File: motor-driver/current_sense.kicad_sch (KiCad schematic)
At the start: 2 parts, among them U19 INA240A1PWR

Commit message: routing complete
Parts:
- C_bypass2: renamed from C_bypass1; footprint (none) -> Capacitor_SMD:C_0603_1608Metric
- renumbered U19 to U20
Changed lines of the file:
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@@
 		(dnp no)
 		(fields_autoplaced yes)
-		(property "Reference" "C_bypass1"
+		(property "Reference" "C_bypass2"
 			(at 194.31 90.1699 0)
 			(effects
@@
 			)
 		)
-		(property "Footprint" ""
+		(property "Footprint" "Capacitor_SMD:C_0603_1608Metric"
 			(at 191.4652 95.25 0)
 			(effects
@@
 			(project "motor-driver"
 				(path "/2980fc7e-b297-4843-ba9f-cceafa384b2f/d36b7053-ee22-4492-bdec-8a6a56460e2b/66c4064f-6677-423e-92fa-0fdb45cd4b17"
-					(reference "C_bypass1")
+					(reference "C_bypass2")
 					(unit 1)
 				)
 				(path "/2980fc7e-b297-4843-ba9f-cceafa384b2f/d36b7053-ee22-4492-bdec-8a6a56460e2b/7d8ebe4c-0ee3-4602-8190-2918d9e2b81c"
-					(reference "C_bypass2")
+					(reference "C_bypass3")
 					(unit 1)
 				)
@@
 		(dnp no)
 		(fields_autoplaced yes)
-		(property "Reference" "U19"
+		(property "Reference" "U20"
 			(at 153.67 86.6392 0)
 			(effects
@@
 			(project "motor-driver"
 				(path "/2980fc7e-b297-4843-ba9f-cceafa384b2f/d36b7053-ee22-4492-bdec-8a6a56460e2b/66c4064f-6677-423e-92fa-0fdb45cd4b17"
-					(reference "U19")
+					(reference "U20")
 					(unit 1)
 				)
 				(path "/2980fc7e-b297-4843-ba9f-cceafa384b2f/d36b7053-ee22-4492-bdec-8a6a56460e2b/7d8ebe4c-0ee3-4602-8190-2918d9e2b81c"
-					(reference "U20")
-					(unit 1)
-				)
+					(reference "U21")
+					(unit 1)
+				)

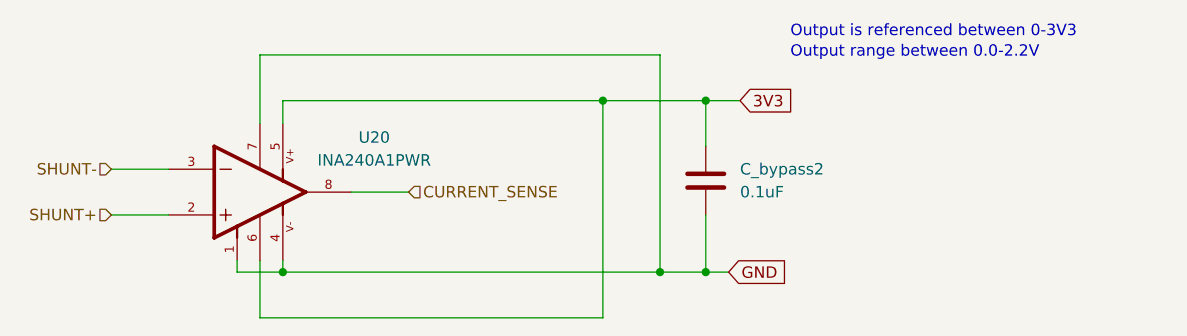
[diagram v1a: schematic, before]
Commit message: added spi connection
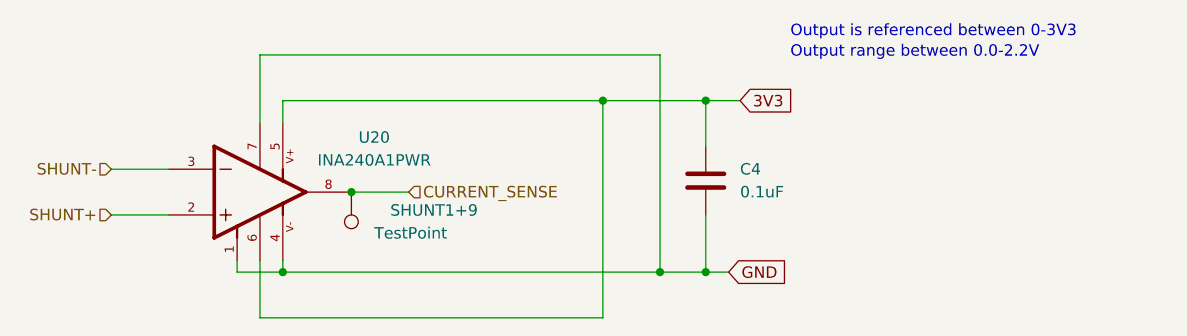
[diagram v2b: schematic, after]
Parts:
- added SHUNT1+9: TestPoint, TestPoint:TestPoint_Loop_D1.80mm_Drill1.0mm_Beaded, symbol Connector:TestPoint
- renumbered C_bypass2 to C4
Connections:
- net CURRENT_SENSE: now also SHUNT1+9.1
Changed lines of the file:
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@@
+	)
+	(junction
+		(at 151.13 92.71)
+		(diameter 0)
+		(color 0 0 0 0)
 	)
 	(junction
@@
 		(dnp no)
 		(fields_autoplaced yes)
-		(property "Reference" "C_bypass2"
+		(property "Reference" "C4"
 			(at 194.31 90.1699 0)
 			(effects
@@
 			(project "motor-driver"
 				(path "/2980fc7e-b297-4843-ba9f-cceafa384b2f/d36b7053-ee22-4492-bdec-8a6a56460e2b/66c4064f-6677-423e-92fa-0fdb45cd4b17"
-					(reference "C_bypass2")
+					(reference "C4")
 					(unit 1)
 				)
 				(path "/2980fc7e-b297-4843-ba9f-cceafa384b2f/d36b7053-ee22-4492-bdec-8a6a56460e2b/7d8ebe4c-0ee3-4602-8190-2918d9e2b81c"
-					(reference "C_bypass3")
+					(reference "C5")
 					(unit 1)
 				)
 				(path "/2980fc7e-b297-4843-ba9f-cceafa384b2f/d36b7053-ee22-4492-bdec-8a6a56460e2b/f72d9f77-0bf6-4a4a-add0-5e2372bd6839"
-					(reference "C_bypass1")
+					(reference "C3")
 					(unit 1)
 				)
@@
 					(unit 1)
 				)
+			)
+		)
+	)
+	(symbol
+		(lib_id "Connector:TestPoint")
+		(at 151.13 92.71 180)
+		(unit 1)
+		(exclude_from_sim no)
+		(in_bom no)
+		(on_board yes)
+		(dnp no)
+		(property "Reference" "SHUNT1+9"
+			(at 155.448 94.742 0)
+			(effects
+				(font
+					(size 1.27 1.27)
+				)
+				(justify right)
+			)
+		)
+		(property "Value" "TestPoint"
+			(at 153.67 97.2819 0)
+			(effects
+				(font
+					(size 1.27 1.27)
+				)
+				(justify right)
+			)
+		)
+		(property "Footprint" "TestPoint:TestPoint_Loop_D1.80mm_Drill1.0mm_Beaded"
+			(at 146.05 92.71 0)
+			(effects
+				(font
+					(size 1.27 1.27)
+				)
+				(hide yes)
+			)
+		)
+		(property "Datasheet" "~"
+			(at 146.05 92.71 0)
+			(effects
+				(font
+					(size 1.27 1.27)
+				)
+				(hide yes)
+			)
+		)
+		(property "Description" "test point"
+			(at 151.13 92.71 0)
+			(effects
+				(font
+					(size 1.27 1.27)
+				)
+				(hide yes)
+			)
+		)
+		(pin "1"
+		)
+		(instances
+			(project "motor-driver"
+				(path "/2980fc7e-b297-4843-ba9f-cceafa384b2f/d36b7053-ee22-4492-bdec-8a6a56460e2b/66c4064f-6677-423e-92fa-0fdb45cd4b17"
+					(reference "SHUNT1+9")
+					(unit 1)
+				)
+				(path "/2980fc7e-b297-4843-ba9f-cceafa384b2f/d36b7053-ee22-4492-bdec-8a6a56460e2b/7d8ebe4c-0ee3-4602-8190-2918d9e2b81c"
+					(reference "SHUNT1+12")
+					(unit 1)
+				)
+				(path "/2980fc7e-b297-4843-ba9f-cceafa384b2f/d36b7053-ee22-4492-bdec-8a6a56460e2b/f72d9f77-0bf6-4a4a-add0-5e2372bd6839"
+					(reference "SENSE1")
+					(unit 1)
+				)

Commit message: added test points
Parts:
- removed SHUNT1+9: TestPoint, TestPoint:TestPoint_Loop_D1.80mm_Drill1.0mm_Beaded, symbol Connector:TestPoint
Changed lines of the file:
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@@
-	)
-	(junction
-		(at 151.13 92.71)
-		(diameter 0)
-		(color 0 0 0 0)
 	)
 	(junction
@@
 					(unit 1)
 				)
-			)
-		)
-	)
-	(symbol
-		(lib_id "Connector:TestPoint")
-		(at 151.13 92.71 180)
-		(unit 1)
-		(exclude_from_sim no)
-		(in_bom no)
-		(on_board yes)
-		(dnp no)
-		(property "Reference" "SHUNT1+9"
-			(at 155.448 94.742 0)
-			(effects
-				(font
-					(size 1.27 1.27)
-				)
-				(justify right)
-			)
-		)
-		(property "Value" "TestPoint"
-			(at 153.67 97.2819 0)
-			(effects
-				(font
-					(size 1.27 1.27)
-				)
-				(justify right)
-			)
-		)
-		(property "Footprint" "TestPoint:TestPoint_Loop_D1.80mm_Drill1.0mm_Beaded"
-			(at 146.05 92.71 0)
-			(effects
-				(font
-					(size 1.27 1.27)
-				)
-				(hide yes)
-			)
-		)
-		(property "Datasheet" "~"
-			(at 146.05 92.71 0)
-			(effects
-				(font
-					(size 1.27 1.27)
-				)
-				(hide yes)
-			)
-		)
-		(property "Description" "test point"
-			(at 151.13 92.71 0)
-			(effects
-				(font
-					(size 1.27 1.27)
-				)
-				(hide yes)
-			)
-		)
-		(pin "1"
-		)
-		(instances
-			(project "motor-driver"
-				(path "/2980fc7e-b297-4843-ba9f-cceafa384b2f/d36b7053-ee22-4492-bdec-8a6a56460e2b/66c4064f-6677-423e-92fa-0fdb45cd4b17"
-					(reference "SHUNT1+9")
-					(unit 1)
-				)
-				(path "/2980fc7e-b297-4843-ba9f-cceafa384b2f/d36b7053-ee22-4492-bdec-8a6a56460e2b/7d8ebe4c-0ee3-4602-8190-2918d9e2b81c"
-					(reference "SHUNT1+12")
-					(unit 1)
-				)
-				(path "/2980fc7e-b297-4843-ba9f-cceafa384b2f/d36b7053-ee22-4492-bdec-8a6a56460e2b/f72d9f77-0bf6-4a4a-add0-5e2372bd6839"
-					(reference "SENSE1")
-					(unit 1)
-				)

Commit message: bom finished
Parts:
- C4: value 0.1uF -> 0.1u; MANUFACTURER (none) -> KEMET; MPN (none) -> C0603C104K5RACTU; Supplier (none) -> Digikey
- U20: Availability In Stock -> (none); Check_prices https://www.snapeda.com/parts/INA240A1PWR/Texas+Instruments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 -> (none); Description_1 -4 to 80V, bidirectional, ultra-precise current sense ampli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 -> (none); MPN (none) -> INA240A1PWR; Supplier (none) -> Digikey
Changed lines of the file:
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@@
 			)
 		)
-		(property "Value" "0.1uF"
+		(property "Value" "0.1u"
 			(at 194.31 92.7099 0)
 			(effects
@@
 		)
 		(property "Description" "Unpolarized capacitor"
+			(at 190.5 91.44 0)
+			(effects
+				(font
+					(size 1.27 1.27)
+				)
+				(hide yes)
+			)
+		)
+		(property "MPN" "C0603C104K5RACTU"
+			(at 190.5 91.44 0)
+			(effects
+				(font
+					(size 1.27 1.27)
+				)
+				(hide yes)
+			)
+		)
+		(property "Supplier" "Digikey"
+			(at 190.5 91.44 0)
+			(effects
+				(font
+					(size 1.27 1.27)
+				)
+				(hide yes)
+			)
+		)
+		(property "MANUFACTURER" "KEMET"
 			(at 190.5 91.44 0)
 			(effects
@@
 			)
 		)
-		(property "Check_prices" "https://www.snapeda.com/parts/INA240A1PWR/Texas+Instruments/view-part/?ref=eda"
-			(at 140.97 92.71 0)
-			(effects
-				(font
-					(size 1.27 1.27)
-				)
-				(justify bottom)
-				(hide yes)
-			)
-		)
 		(property "STANDARD" "IPC7351B"
 			(at 140.97 92.71 0)
@@
 			)
 		)
-		(property "Description_1" "-4 to 80V, bidirectional, ultra-precise current sense amplifier with enhanced PWM rejection"
-			(at 140.97 92.71 0)
-			(effects
-				(font
-					(size 1.27 1.27)
-				)
-				(justify bottom)
-				(hide yes)
-			)
-		)
-		(property "Availability" "In Stock"
-			(at 140.97 92.71 0)
-			(effects
-				(font
-					(size 1.27 1.27)
-				)
-				(justify bottom)
-				(hide yes)
-			)
-		)
 		(property "MANUFACTURER" "Texas Instruments"
 			(at 140.97 92.71 0)
@@
 				(hide yes)
 			)
+		)
+		(property "MPN" "INA240A1PWR"
+			(at 140.97 92.71 0)
+			(effects
+				(font
+					(size 1.27 1.27)
+				)
+				(hide yes)
+			)
+		)
+		(property "Supplier" "Digikey"
+			(at 140.97 92.71 0)
+			(effects
+				(font
+					(size 1.27 1.27)
+				)
+				(hide yes)
+			)
